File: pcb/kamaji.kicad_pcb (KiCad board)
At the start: 2 copper layers, 130 x 99 mm, 30 parts, among them J1 RJ10, J2 RJ10, J3 RJ10, J4 RJ10, J5 RJ10, Q1 TIP120, Q2 TIP120, SW1 CTRL1, SW2 CTRL2, SW3 CTRL3, U1 ATMEGA328P-PU

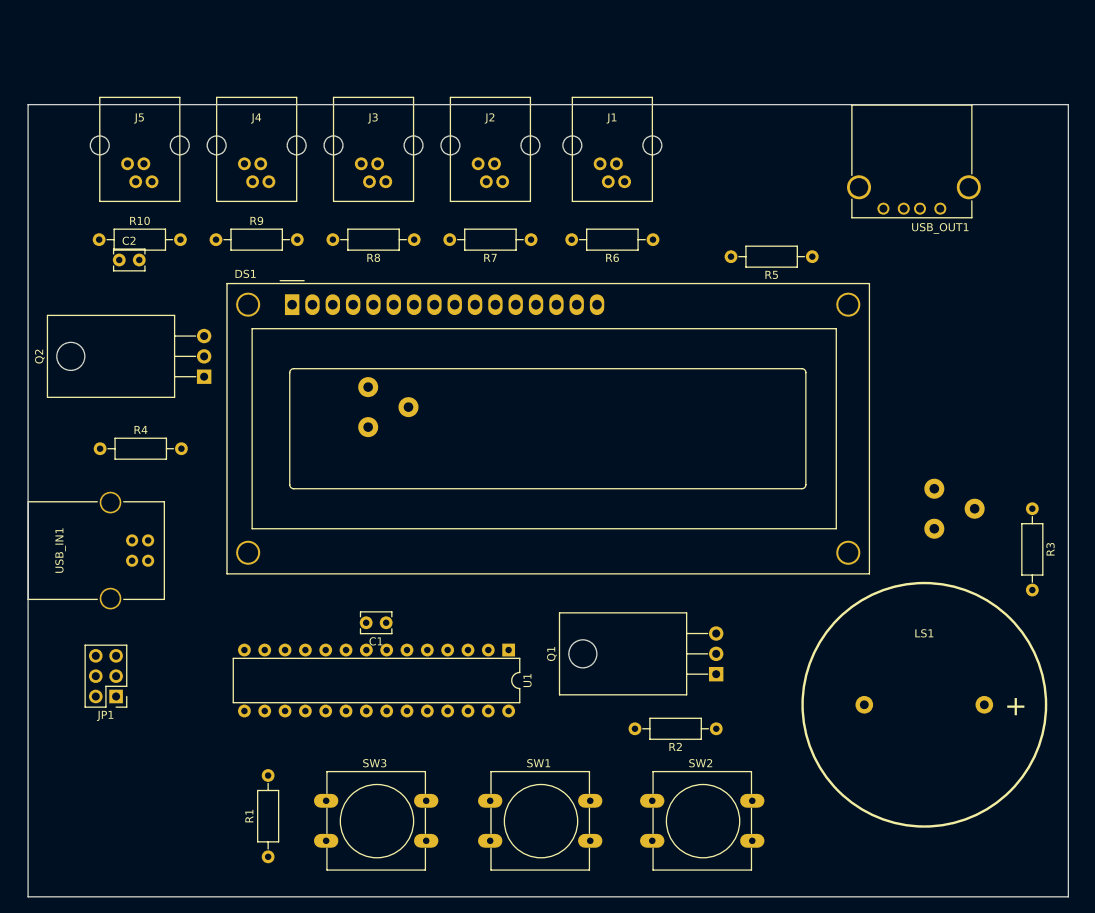
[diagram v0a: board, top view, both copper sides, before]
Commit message: change component placement for easier routing
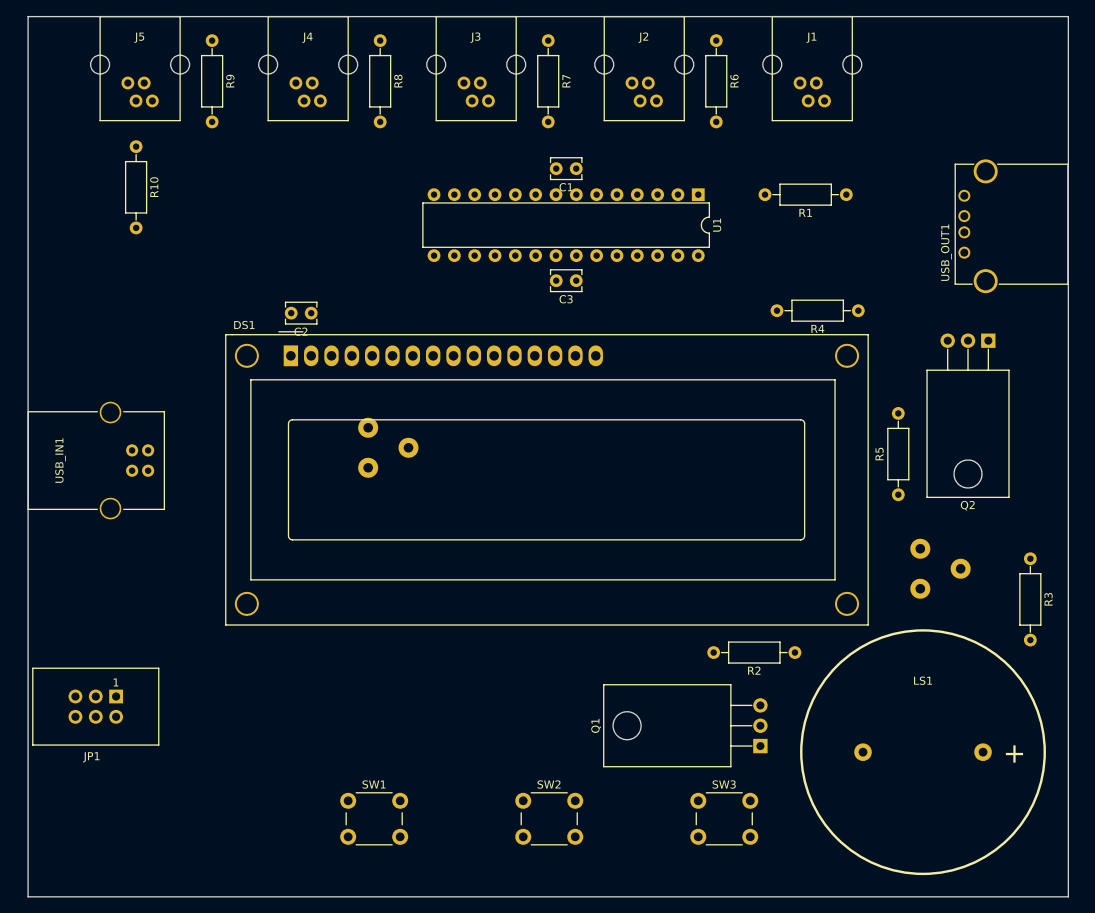
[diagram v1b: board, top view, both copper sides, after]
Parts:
- added C3: 0.1uF, Capacitors_THT:C_Disc_D3.8mm_W2.6mm_P2.50mm, F.Cu at (168.5, 63.0)
- JP1: footprint Pin_Headers:Pin_Header_Straight_2x03_Pitch2.54mm -> Connectors:IDC_Header_Straight_6pins
- SW1, SW2, SW3: footprint Buttons_Switches_THT:SW_PUSH-12mm -> Buttons_Switches_THT:SW_PUSH_6mm_h8.5mm
- moved R1 109.9 mm to (202.2, 52.2), turned to 180 degrees
- moved Q2 98.1 mm to (220.0, 70.5), turned to 180 degrees
- moved R4 96.3 mm to (203.8, 66.8), turned to 180 degrees
- moved U1 61.6 mm to (183.8, 52.2)
- moved C1 61.5 mm to (168.5, 49.0)
- moved SW3 46.5 mm to (183.8, 128.0)
- moved R5 31.6 mm to (208.8, 89.8), turned to 90 degrees
- moved J1 26.9 mm to (198.0, 30.0)
- moved R6 26.1 mm to (186.0, 33.0), turned to 270 degrees
- moved R8 25.2 mm to (144.0, 33.0), turned to 270 degrees
- moved R7 25.0 mm to (165.0, 33.0), turned to 270 degrees
- moved C2 24.9 mm to (135.4, 67.1), turned to 180 degrees
- moved R9 24.9 mm to (123.0, 33.0), turned to 270 degrees
- moved J2 21.7 mm to (177.0, 30.0)
- moved SW1 17.8 mm to (140.0, 128.0)
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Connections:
- C2 pad 1: GND -> VCC
- C2 pad 2: VCC -> GND
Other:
- board size 130 x 99 mm -> 130 x 110 mm

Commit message: a few more component moves
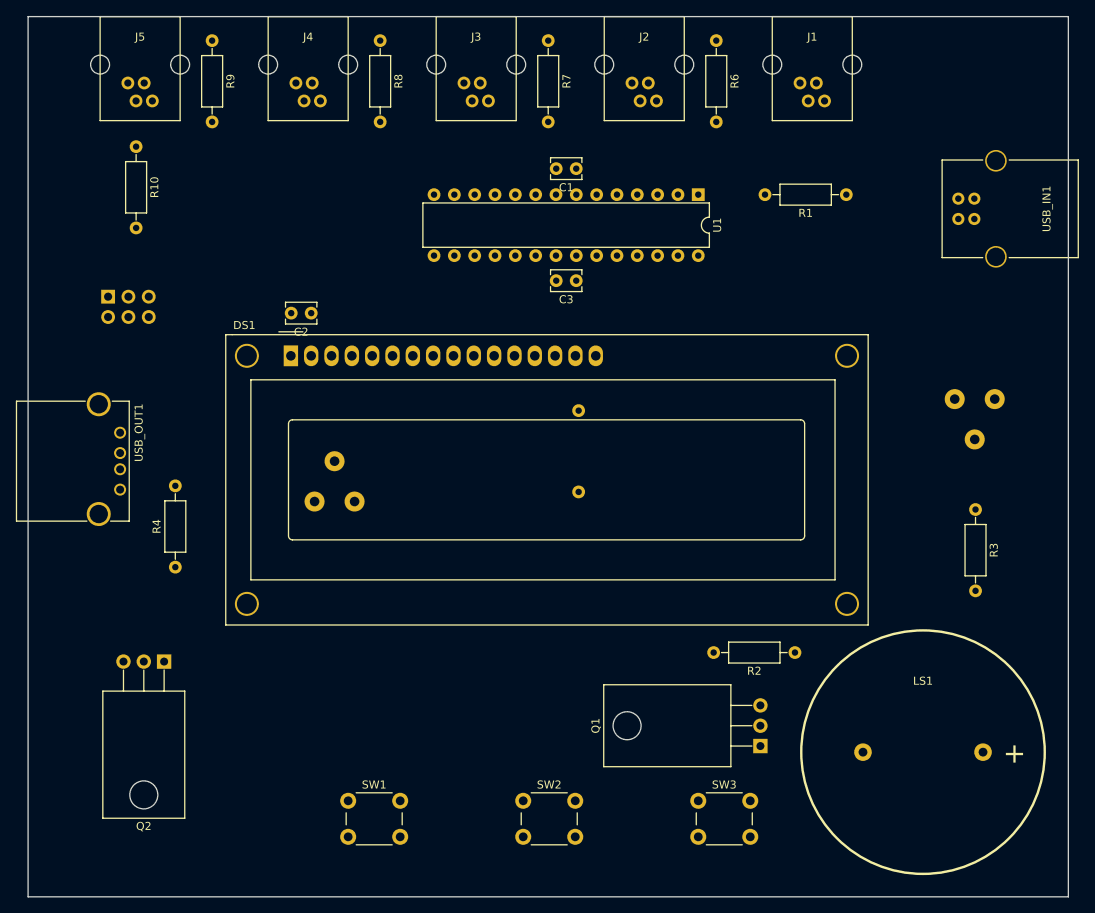
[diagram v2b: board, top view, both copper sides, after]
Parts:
- JP1, R5: moved to B.Cu
- moved Q2 110.5 mm to (117.0, 110.6)
- moved USB_OUT1 107.9 mm to (111.5, 82.0), turned to 270 degrees
- moved USB_IN1 106.8 mm to (216.2, 52.8), turned to 0 degrees
- moved R4 91.2 mm to (118.4, 98.8), turned to 90 degrees
- moved JP1 50.0 mm to (110.0, 65.0), turned to 0 degrees
- moved R5 40.0 mm to (168.8, 89.4)
- moved RV1 24.1 mm to (215.8, 77.8), turned to 0 degrees
- moved R3 9.21 mm to (218.4, 91.6)
- moved RV2 4.55 mm to (140.8, 90.6), turned to 180 degrees

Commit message: define net classes
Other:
- net class Power added: clearance 0.2, trace_width 0.5, via_dia 0.6, via_drill 0.4
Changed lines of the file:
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@@
     (add_net CBTN2)
     (add_net CBTN3)
-    (add_net GND)
     (add_net LAMP)
     (add_net LCD_D0)
@@
     (add_net "Net-(J4-Pad2)")
     (add_net "Net-(J5-Pad2)")
-    (add_net "Net-(LS1-Pad1)")
-    (add_net "Net-(LS1-Pad2)")
     (add_net "Net-(Q1-Pad1)")
     (add_net "Net-(Q2-Pad1)")
@@
     (add_net "Net-(USB_IN1-Pad2)")
     (add_net "Net-(USB_IN1-Pad3)")
-    (add_net "Net-(USB_OUT1-Pad2)")
-    (add_net "Net-(USB_OUT1-Pad3)")
     (add_net PBTN1)
     (add_net PBTN2)
@@
     (add_net SCK)
     (add_net SND)
+  )
+  (net_class Power ""
+    (clearance 0.2)
+    (trace_width 0.5)
+    (via_dia 0.6)
+    (via_drill 0.4)
+    (uvia_dia 0.3)
+    (uvia_drill 0.1)
+    (add_net GND)
+    (add_net "Net-(LS1-Pad1)")
+    (add_net "Net-(LS1-Pad2)")
+    (add_net "Net-(USB_OUT1-Pad2)")
+    (add_net "Net-(USB_OUT1-Pad3)")
     (add_net VCC)
   )

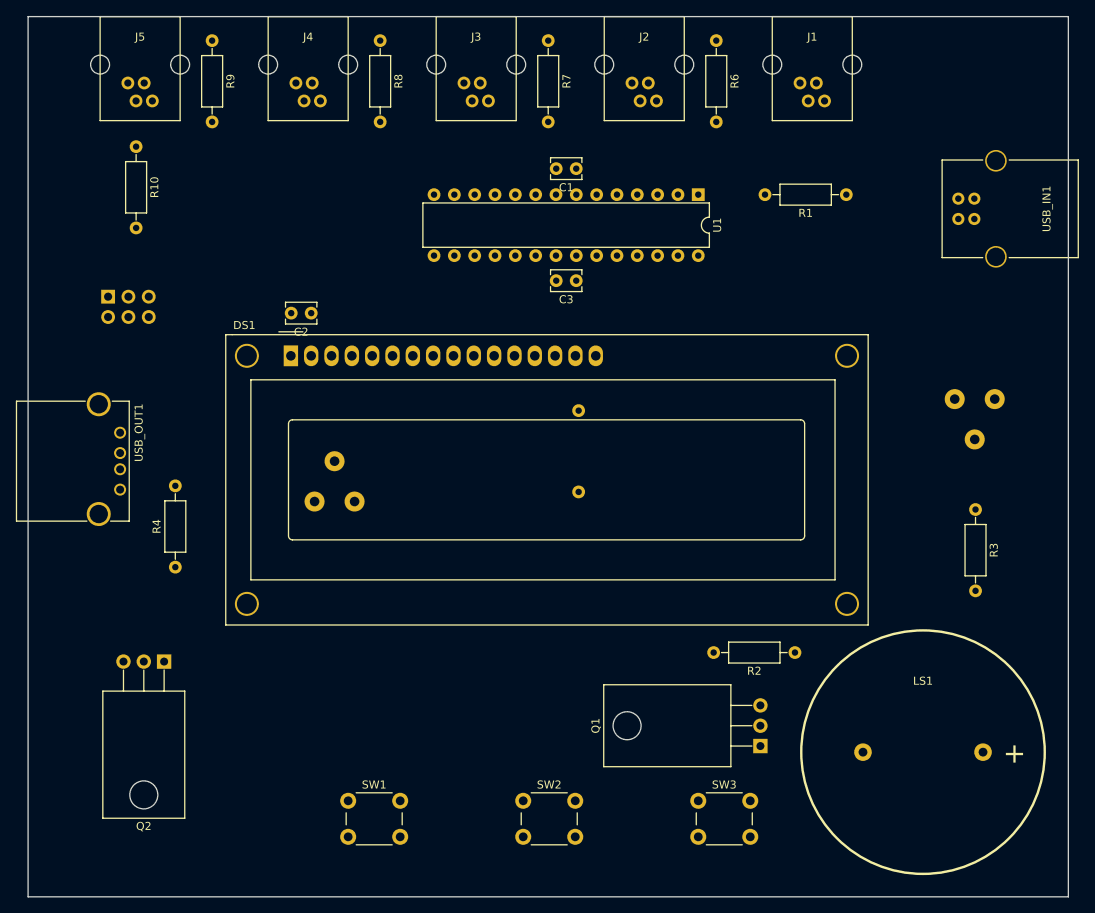
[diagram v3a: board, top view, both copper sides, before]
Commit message: start drawing traces
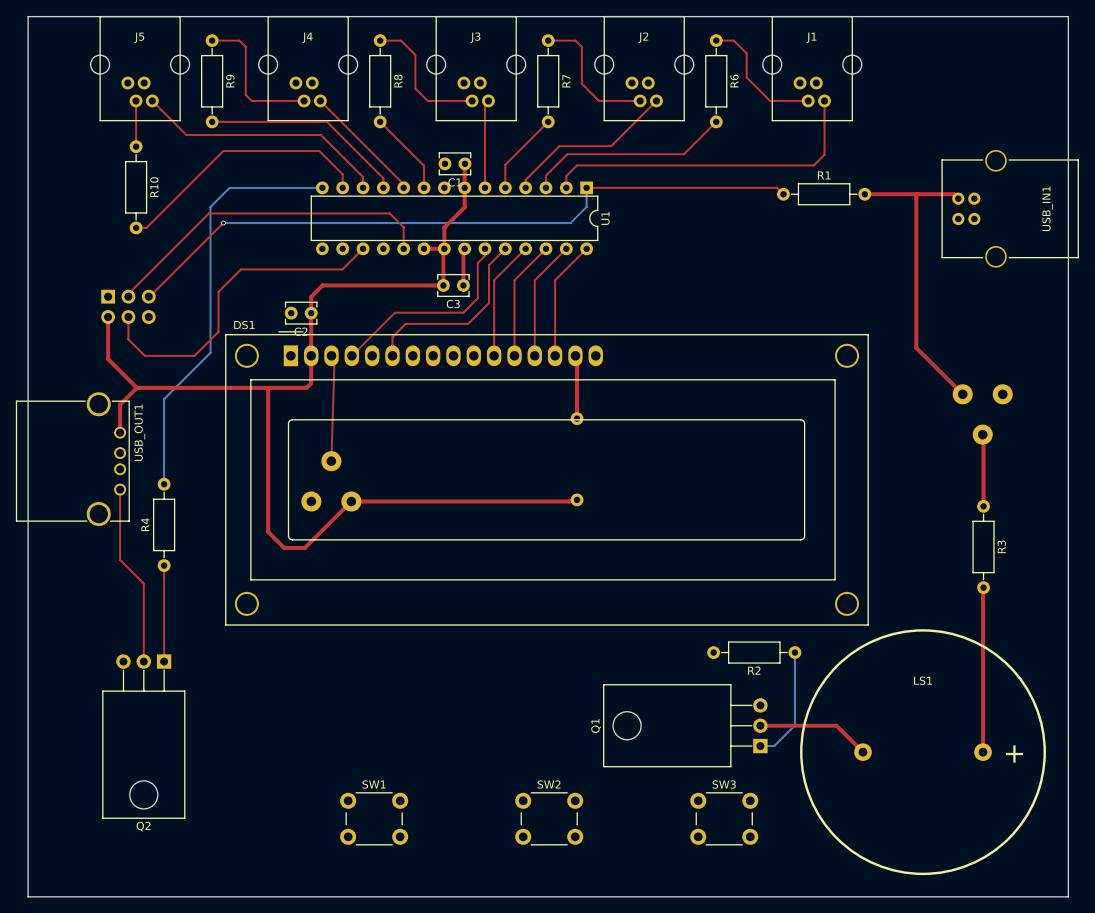
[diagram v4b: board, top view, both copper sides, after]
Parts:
- moved C3 14.1 mm to (154.4, 63.6)
- moved U1 14.0 mm to (169.8, 51.4)
- moved C1 13.9 mm to (154.6, 48.4)
- moved R1 7.85 mm to (194.4, 52.2), turned to 0 degrees
- moved R4 1.41 mm to (117.0, 98.6)
- moved RV1 1.17 mm to (216.8, 77.2)
- moved R3 1.08 mm to (219.4, 91.2)
- moved R5 1.02 mm to (168.6, 90.4)
- moved RV2 0.40 mm to (140.4, 90.6)
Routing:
- net VCC: track 0.00 -> 184.8 mm
- net RST: track 0.00 -> 86.8 mm, vias 0 -> 1
- net LAMP: track 0.00 -> 52.0 mm
- net SCK: track 0.00 -> 42.3 mm
- net PBTN1: track 0.00 -> 41.6 mm
- net CBTN2: track 0.00 -> 41.4 mm
- net PLED5: track 0.00 -> 32.7 mm
- net PBTN5: track 0.00 -> 31.6 mm
- net PLED1: track 0.00 -> 25.6 mm
- net PLED4: track 0.00 -> 25.5 mm
- net LCD_RS: track 0.00 -> 25.3 mm
- net LCD_EN: track 0.00 -> 23.8 mm
- net Net-(Q2-Pad2): track 0.00 -> 22.7 mm
- net PBTN2: track 0.00 -> 21.4 mm
- net Net-(LS1-Pad1): track 0.00 -> 20.6 mm
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
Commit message: first attempt at PCB routing
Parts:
- moved J5 6.00 mm to (120.0, 30.0)
- moved R9 5.56 mm to (128.5, 33.8)
- moved J4 5.00 mm to (140.0, 30.0)
- moved R8 4.67 mm to (148.6, 33.8)
- moved J3 4.00 mm to (160.0, 30.0)
- moved R7 3.88 mm to (168.8, 33.8)
- moved J2 3.00 mm to (180.0, 30.0)
- moved R6 2.82 mm to (188.7, 33.8)
- moved J1 2.00 mm to (200.0, 30.0)
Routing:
- net CBTN3: track 0.00 -> 142.0 mm, vias 0 -> 1
- net SND: track 0.00 -> 100.6 mm
- net CBTN2: track 41.4 -> 140.3 mm
- net CBTN1: track 0.00 -> 86.9 mm
- net VCC: track 184.8 -> 248.8 mm, vias 0 -> 1
- net GND: track 4.65 -> 18.1 mm
- net PLED4: track 25.5 -> 19.0 mm
- net Net-(J4-Pad2): track 18.1 -> 13.8 mm
- net PBTN5: track 31.6 -> 27.3 mm
- net PLED2: track 10.5 -> 14.3 mm
- net PBTN2: track 21.4 -> 25.2 mm
- net Net-(J2-Pad2): track 17.3 -> 13.5 mm
- net Net-(J3-Pad2): track 17.1 -> 13.7 mm
- net PLED5: track 32.7 -> 29.9 mm
- net Net-(J1-Pad2): track 16.4 -> 13.6 mm
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- added copper zone on B.Cu, net GND
- added copper zone on F.Cu, net GND
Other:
- board text added: "Кнопочная Система v1.0 Илья Струков <iley@iley.ru>"

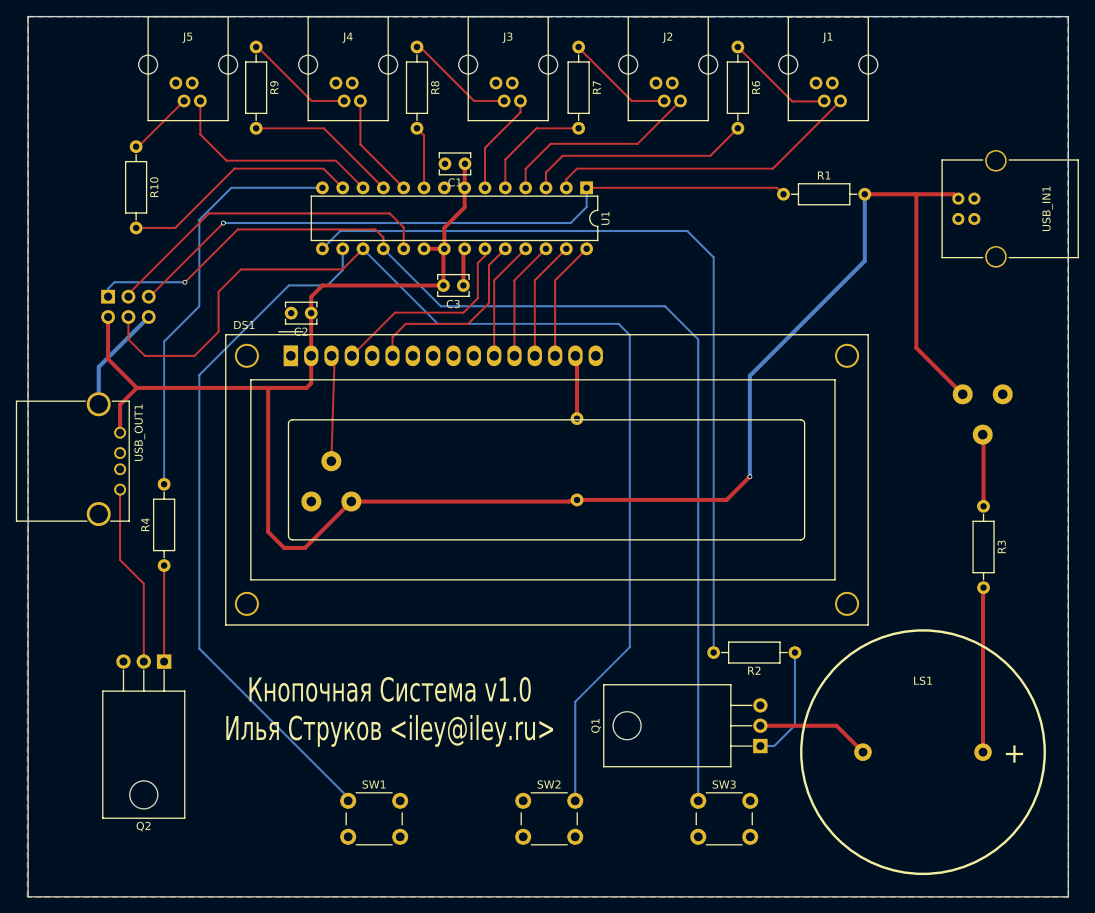
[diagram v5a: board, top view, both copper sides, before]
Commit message: a few minor changes to the PCB layout
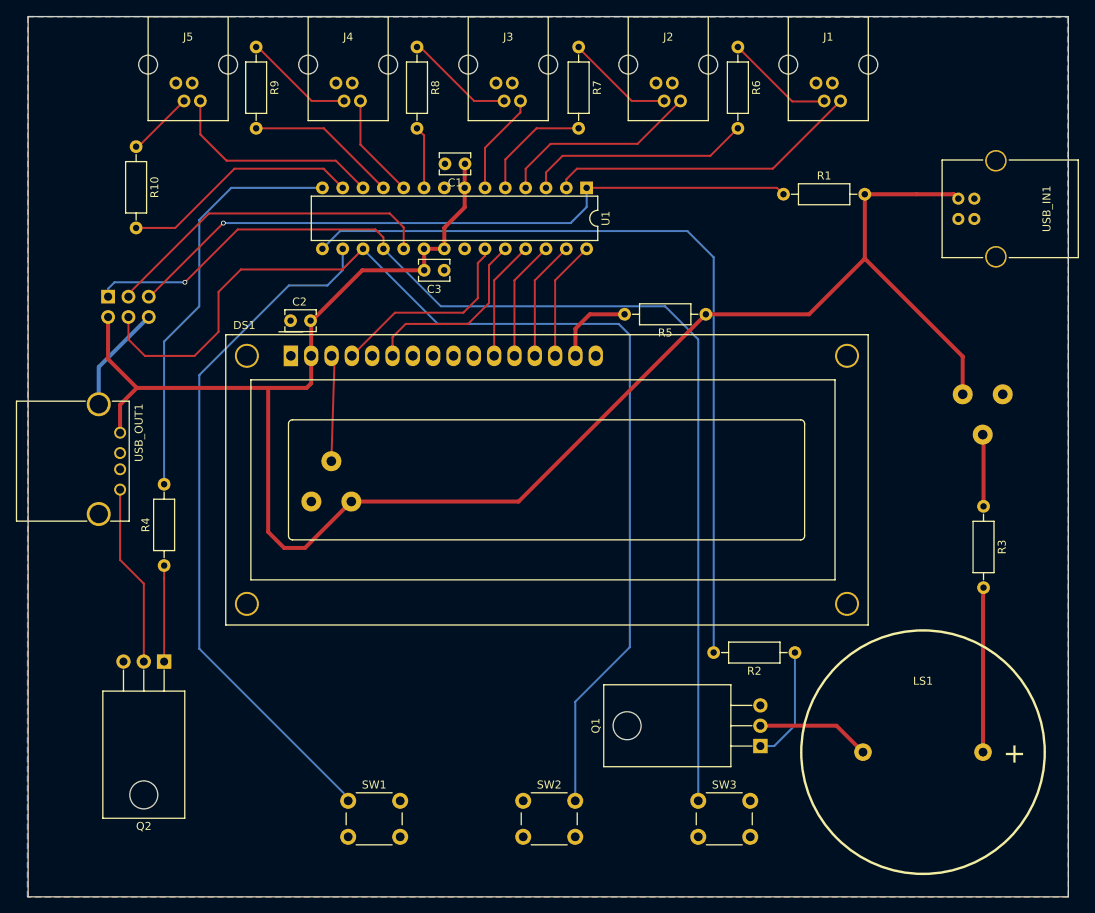
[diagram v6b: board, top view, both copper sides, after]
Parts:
- R5: moved to F.Cu
- moved R5 28.2 mm to (184.7, 67.2), turned to 180 degrees
- moved C3 3.06 mm to (152.0, 61.7)
- moved C2 0.95 mm to (135.3, 68.0)
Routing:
- net VCC: track 248.8 -> 230.8 mm, vias 1 -> 0
- net GND: track 18.1 -> 13.7 mm
- net Net-(DS1-Pad15): track 8.49 -> 11.1 mm
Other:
- board text removed: "Кнопочная Система v1.0 Илья Струков <iley@iley.ru>"
